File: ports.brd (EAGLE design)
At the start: 24 x 10 mm, 3 parts

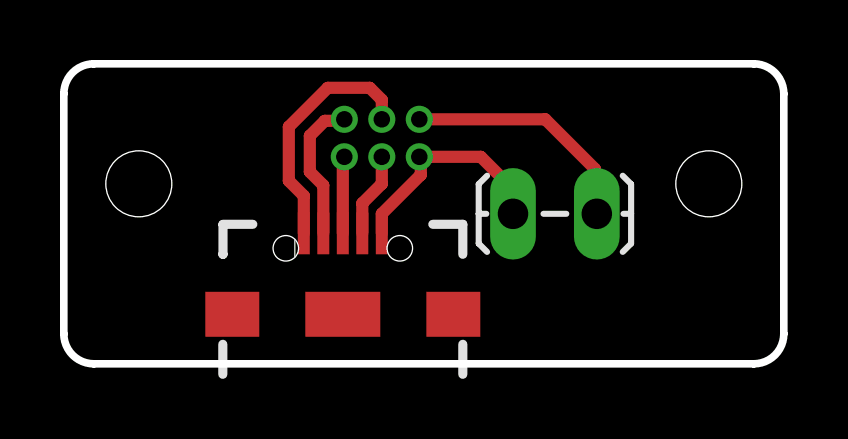
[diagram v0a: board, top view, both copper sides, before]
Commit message: Updated ports board
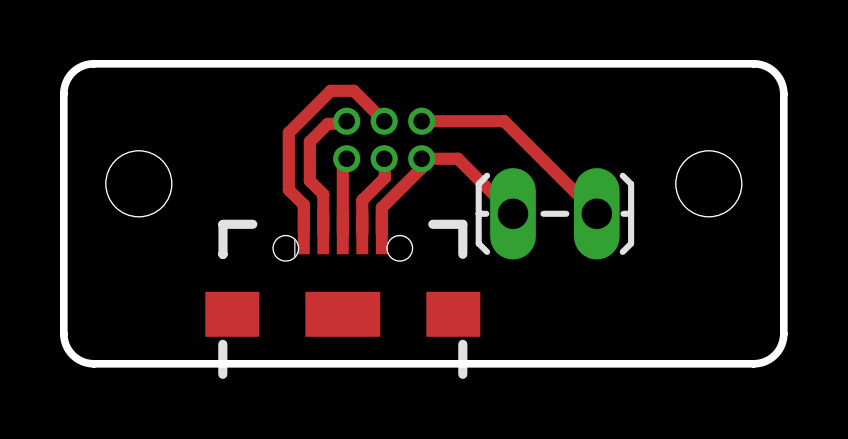
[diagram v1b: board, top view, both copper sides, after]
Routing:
- net VBATT: track 8.06 -> 7.11 mm
- net GND: track 7.50 -> 6.84 mm
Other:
- board text added: "Thickness = 1.6"
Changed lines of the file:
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@@
 <hole x="2.5" y="6" drill="2.2"/>
 <hole x="21.5" y="6" drill="2.2"/>
+<dimension x1="0" y1="0" x2="24" y2="0" x3="12" y3="-3.7" textsize="1.778" layer="51" dtype="horizontal"/>
+<dimension x1="5" y1="0" x2="19" y2="0" x3="12" y3="15.5" textsize="1.778" layer="51" dtype="horizontal"/>
+<dimension x1="0" y1="10" x2="0" y2="0" x3="-1.6" y3="5" textsize="1.778" layer="51" dtype="vertical"/>
+<text x="-14.5" y="13.4" size="1.778" layer="51">Thickness = 1.6</text>
+<dimension x1="20.4" y1="6" x2="22.6" y2="6" x3="21.5" y3="7.3" textsize="1.778" layer="51" dtype="diameter"/>
+<dimension x1="2.5" y1="6" x2="2.5" y2="0" x3="3.6" y3="3" textsize="1.778" layer="51" dtype="vertical"/>
+<dimension x1="21.5" y1="6" x2="24" y2="6" x3="22.75" y3="3" textsize="1.778" layer="51" dtype="horizontal"/>
 </plain>
 <attributes>
@@
 <contactref element="U$4" pad="GND1"/>
 <contactref element="U$1" pad="P4"/>
-<wire x1="10.6" y1="4.35" x2="10.6" y2="5" width="0.4064" layer="1"/>
-<wire x1="10.6" y1="5" x2="11.9" y2="6.3" width="0.4064" layer="1"/>
-<wire x1="11.9" y1="6.3" x2="11.9" y2="6.85" width="0.4064" layer="1"/>
-<wire x1="11.9" y1="6.85" x2="11.85" y2="6.9" width="0.4064" layer="1"/>
-<wire x1="14.973" y1="5.827" x2="13.9" y2="6.9" width="0.4064" layer="1"/>
-<wire x1="13.9" y1="6.9" x2="11.85" y2="6.9" width="0.4064" layer="1"/>
 <contactref element="JP1" pad="1"/>
-<wire x1="14.973" y1="5.827" x2="14.973" y2="5" width="0.4064" layer="1"/>
+<wire x1="11.93" y1="6.835" x2="13.138" y2="6.835" width="0.4064" layer="1"/>
+<wire x1="13.138" y1="6.835" x2="14.973" y2="5" width="0.4064" layer="1"/>
+<wire x1="11.93" y1="6.835" x2="11.93" y2="6.53" width="0.4064" layer="1"/>
+<wire x1="11.93" y1="6.53" x2="10.6" y2="5.2" width="0.4064" layer="1"/>
+<wire x1="10.6" y1="5.2" x2="10.6" y2="4.35" width="0.4064" layer="1"/>
 </signal>
 <signal name="D+">
 <contactref element="U$4" pad="D+1"/>
 <contactref element="U$1" pad="P6"/>
-<wire x1="9.3" y1="4.35" x2="9.3" y2="6.85" width="0.4064" layer="1"/>
-<wire x1="9.3" y1="6.85" x2="9.35" y2="6.9" width="0.4064" layer="1"/>
+<wire x1="9.3" y1="4.35" x2="9.3" y2="6.705" width="0.4064" layer="1"/>
+<wire x1="9.3" y1="6.705" x2="9.43" y2="6.835" width="0.4064" layer="1"/>
 </signal>
 <signal name="D-">
 <contactref element="U$4" pad="D-1"/>
 <contactref element="U$1" pad="P3"/>
-<wire x1="8.65" y1="4.35" x2="8.65" y2="5.95" width="0.4064" layer="1"/>
-<wire x1="8.65" y1="5.95" x2="8.2" y2="6.4" width="0.4064" layer="1"/>
-<wire x1="8.2" y1="6.4" x2="8.2" y2="7.6" width="0.4064" layer="1"/>
-<wire x1="8.2" y1="7.6" x2="8.7" y2="8.1" width="0.4064" layer="1"/>
-<wire x1="8.7" y1="8.1" x2="9.3" y2="8.1" width="0.4064" layer="1"/>
-<wire x1="9.3" y1="8.1" x2="9.35" y2="8.15" width="0.4064" layer="1"/>
+<wire x1="8.65" y1="4.35" x2="8.65" y2="5.65" width="0.4064" layer="1"/>
+<wire x1="8.65" y1="5.65" x2="8.2" y2="6.1" width="0.4064" layer="1"/>
+<wire x1="8.2" y1="6.1" x2="8.2" y2="7.4" width="0.4064" layer="1"/>
+<wire x1="8.2" y1="7.4" x2="8.8" y2="8" width="0.4064" layer="1"/>
+<wire x1="8.8" y1="8" x2="9.345" y2="8" width="0.4064" layer="1"/>
+<wire x1="9.345" y1="8" x2="9.43" y2="8.085" width="0.4064" layer="1"/>
 </signal>
 <signal name="VBUS">
 <contactref element="U$4" pad="VBUS1"/>
 <contactref element="U$1" pad="P2"/>
-<wire x1="8" y1="4.35" x2="8" y2="5.6" width="0.4064" layer="1"/>
-<wire x1="8" y1="5.6" x2="7.5" y2="6.1" width="0.4064" layer="1"/>
-<wire x1="7.5" y1="6.1" x2="7.5" y2="7.9" width="0.4064" layer="1"/>
-<wire x1="7.5" y1="7.9" x2="8.8" y2="9.2" width="0.4064" layer="1"/>
-<wire x1="8.8" y1="9.2" x2="10.2" y2="9.2" width="0.4064" layer="1"/>
-<wire x1="10.2" y1="9.2" x2="10.6" y2="8.8" width="0.4064" layer="1"/>
-<wire x1="10.6" y1="8.8" x2="10.6" y2="8.15" width="0.4064" layer="1"/>
+<wire x1="8" y1="4.35" x2="8" y2="5.3" width="0.4064" layer="1"/>
+<wire x1="8" y1="5.3" x2="7.5" y2="5.8" width="0.4064" layer="1"/>
+<wire x1="7.5" y1="5.8" x2="7.5" y2="7.7" width="0.4064" layer="1"/>
+<wire x1="7.5" y1="7.7" x2="8.9" y2="9.1" width="0.4064" layer="1"/>
+<wire x1="8.9" y1="9.1" x2="9.665" y2="9.1" width="0.4064" layer="1"/>
+<wire x1="9.665" y1="9.1" x2="10.68" y2="8.085" width="0.4064" layer="1"/>
 </signal>
 <signal name="ID">
 <contactref element="U$4" pad="ID1"/>
 <contactref element="U$1" pad="P5"/>
-<wire x1="9.95" y1="4.35" x2="9.95" y2="5.35" width="0.4064" layer="1"/>
-<wire x1="9.95" y1="5.35" x2="10.6" y2="6" width="0.4064" layer="1"/>
-<wire x1="10.6" y1="6" x2="10.6" y2="6.9" width="0.4064" layer="1"/>
+<wire x1="9.95" y1="4.35" x2="9.95" y2="5.45" width="0.4064" layer="1"/>
+<wire x1="9.95" y1="5.45" x2="10.7" y2="6.2" width="0.4064" layer="1"/>
+<wire x1="10.7" y1="6.2" x2="10.7" y2="6.815" width="0.4064" layer="1"/>
+<wire x1="10.7" y1="6.815" x2="10.68" y2="6.835" width="0.4064" layer="1"/>
 </signal>
 <signal name="VBATT">
 <contactref element="JP1" pad="2"/>
 <contactref element="U$1" pad="P1"/>
-<wire x1="11.85" y1="8.15" x2="16.05" y2="8.15" width="0.4064" layer="1"/>
-<wire x1="16.05" y1="8.15" x2="17.7" y2="6.5" width="0.4064" layer="1"/>
-<wire x1="17.7" y1="6.5" x2="17.7" y2="5.067" width="0.4064" layer="1"/>
-<wire x1="17.7" y1="5.067" x2="17.767" y2="5" width="0.4064" layer="1"/>
+<wire x1="11.93" y1="8.085" x2="14.682" y2="8.085" width="0.4064" layer="1"/>
+<wire x1="14.682" y1="8.085" x2="17.767" y2="5" width="0.4064" layer="1"/>
 </signal>
 </signals>
